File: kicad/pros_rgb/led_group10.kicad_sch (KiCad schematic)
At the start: 8 parts

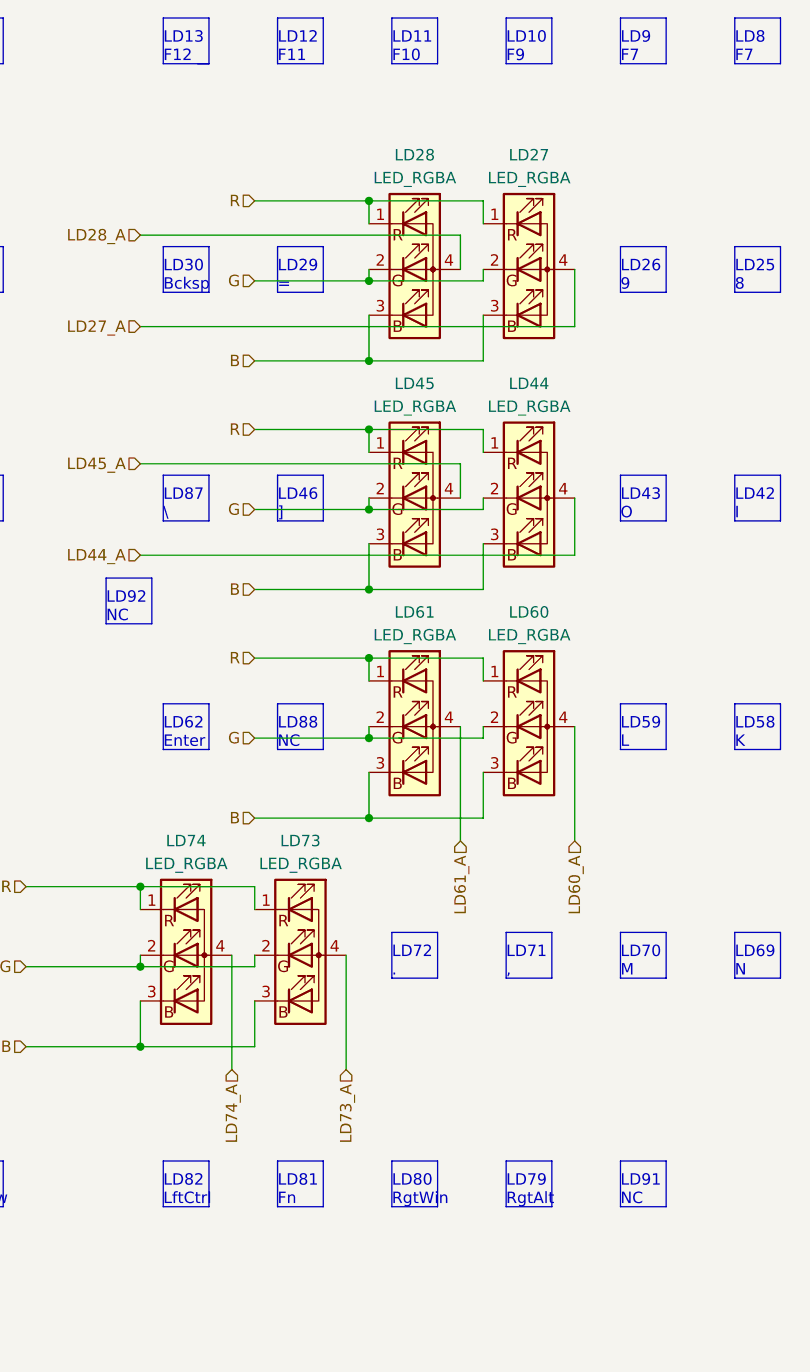
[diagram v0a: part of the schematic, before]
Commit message: kicad/pros_rgb: fix typos
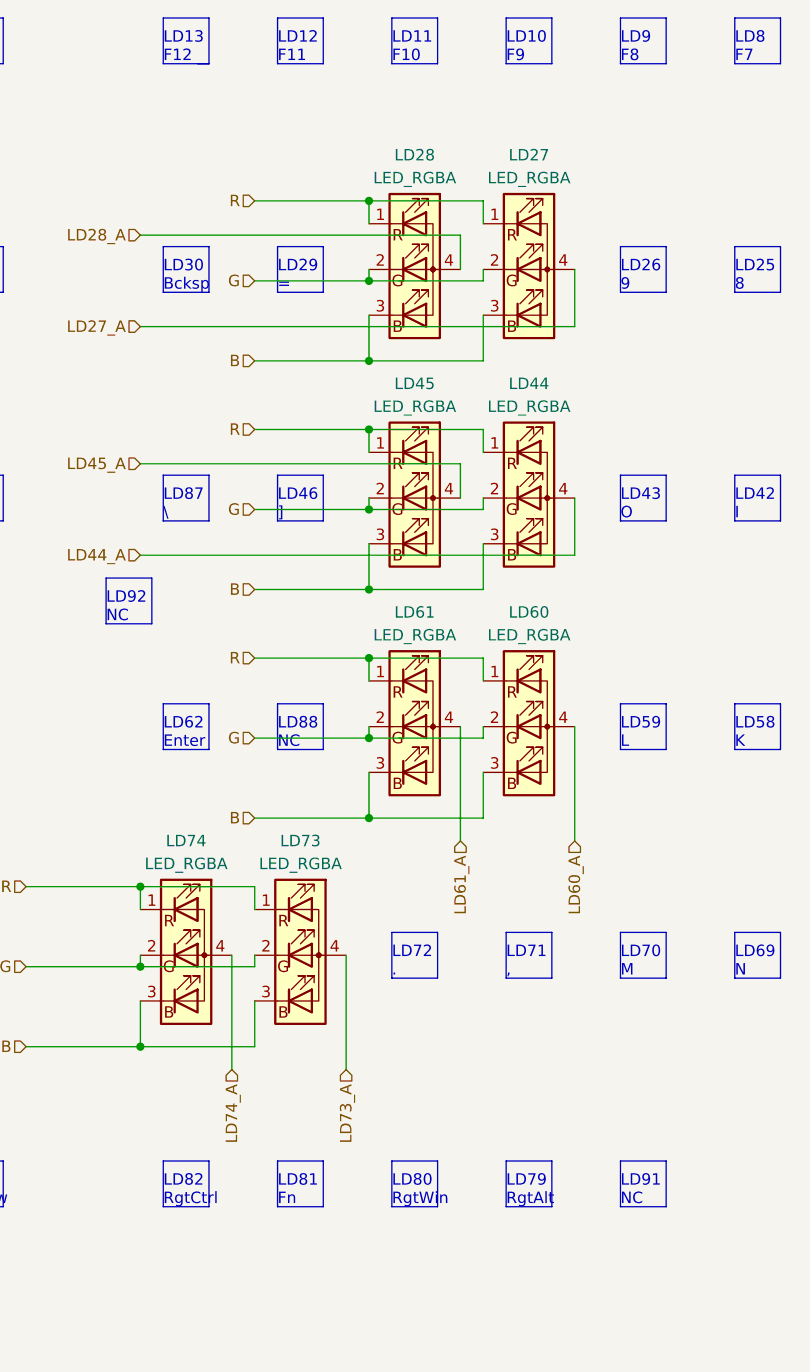
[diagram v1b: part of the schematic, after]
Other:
- note added: "LD82 RgtCtrl"
- note added: "LD9 F8"
- note removed: "LD82 LftCtrl"
- note removed: "LD9 F7"
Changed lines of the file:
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@@
     (stroke (width 0) (type default) (color 0 0 0 0))
   )
-  (text "LD82\nLftCtrl" (at 106.68 156.21 0)
+  (text "LD82\nRgtCtrl" (at 106.68 156.21 0)
     (effects (font (size 1.27 1.27)) (justify left bottom))
   )
@@
     (effects (font (size 1.27 1.27)) (justify left bottom))
   )
-  (text "LD9\nF7" (at 157.48 29.21 0)
+  (text "LD9\nF8" (at 157.48 29.21 0)
     (effects (font (size 1.27 1.27)) (justify left bottom))
   )
